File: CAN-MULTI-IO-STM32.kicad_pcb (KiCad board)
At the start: 2 copper layers, 81 x 55 mm, 42 parts, among them J1 H GND L, J2 TERM, J3 UART1, J4 SWLINK, J5 PWR IN, U1 STM32L433RCT3, U2 MCP2562-E-SN

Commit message: schematic and layout refinement
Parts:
- removed CONSW3, CONSW4: Conn_01x05, Connector_PinHeader_2.54mm:PinHeader_1x05_P2.54mm_Horizontal
- added I2C2: G SCL SDA 3V, Connector_PinHeader_2.54mm:PinHeader_1x04_P2.54mm_Horizontal, F.Cu at (139.2, 88.0)
- added J7: I2C PU EN, Connector_PinHeader_2.54mm:PinHeader_1x02_P2.54mm_Vertical, F.Cu at (149.1, 92.0)
- added ONEWIRE1: G OW 3V, Connector_PinHeader_2.54mm:PinHeader_1x03_P2.54mm_Horizontal, F.Cu at (154.5, 88.0)
- added RPU1: 4K7, Resistor_SMD:R_0603_1608Metric_Pad0.98x0.95mm_HandSolder, F.Cu at (145.3, 91.0)
- added RPU2: 4K7, Resistor_SMD:R_0603_1608Metric_Pad0.98x0.95mm_HandSolder, F.Cu at (145.3, 92.8)
- added RPU3: 4K7, Resistor_SMD:R_0603_1608Metric_Pad0.98x0.95mm_HandSolder, F.Cu at (159.0, 90.8)
- renumbered ANA_IN1 to ADIO1, ANA_IN2 to ADIO2
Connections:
- U1 pad 17: /ADC1_IN8 -> unconnected-(U1-PA3-Pad17)
- U1 pad 20: /ADC1_IN9 -> unconnected-(U1-PA4-Pad20)
- U1 pad 21: /ADC1_IN10 -> unconnected-(U1-PA5-Pad21)
- U1 pad 22: /ADC1_IN11 -> unconnected-(U1-PA6-Pad22)
- U1 pad 23: /ADC1_IN12 -> unconnected-(U1-PA7-Pad23)
- U1 pad 24: unconnected-(U1-PC4-Pad24) -> /ONEW
- U1 pad 29: unconnected-(U1-PB10-Pad29) -> /I2C2_SCL
- U1 pad 30: unconnected-(U1-PB11-Pad30) -> /I2C2_SDA
- U1 pad 50: /DEN4 -> unconnected-(U1-PA15-Pad50)
- U1 pad 52: /CTL4 -> unconnected-(U1-PC11-Pad52)
- U1 pad 54: /DEN3 -> unconnected-(U1-PD2-Pad54)
- U1 pad 57: /CTL3 -> unconnected-(U1-PB5-Pad57)
- U1 pad 61: /CTL2 -> unconnected-(U1-PB8-Pad61)
- U1 pad 62: /DEN2 -> unconnected-(U1-PB9-Pad62)
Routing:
- net +3.3V: track 163.5 -> 207.8 mm
- net /ONEW: track 0.00 -> 32.0 mm, vias 0 -> 1
- net /I2C2_SCL: track 0.00 -> 25.9 mm, vias 0 -> 1
- net /I2C2_SDA: track 0.00 -> 23.4 mm, vias 0 -> 1
- net Net-(J7-Pin_1): track 0.00 -> 4.99 mm
- net /ADC1_IN10: track 1.72 -> 0.00 mm, vias 1 -> 0
- net /ADC1_IN12: track 1.69 -> 0.00 mm, vias 1 -> 0
- net /ADC1_IN11: track 1.69 -> 0.00 mm, vias 1 -> 0
- net /ADC1_IN9: track 1.19 -> 0.00 mm, vias 1 -> 0
- net GND: vias 88 -> 106

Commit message: final tweaks
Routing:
- net GND: track 5.06 -> 0.00 mm
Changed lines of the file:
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@@
 		)
 	)
-	(segment
-		(start 137 94.75)
-		(end 137.25 94.5)
-		(width 0.254)
-		(layer "F.Cu")
-		(net 6)
-	)
-	(segment
-		(start 138.575 91.9)
-		(end 138.575 92.775)
-		(width 0.254)
-		(layer "F.Cu")
-		(net 6)
-	)
-	(segment
-		(start 137 95.9)
-		(end 137 94.75)
-		(width 0.254)
-		(layer "F.Cu")
-		(net 6)
-	)
-	(segment
-		(start 138.225 93.125)
-		(end 138.225 93.75)
-		(width 0.254)
-		(layer "F.Cu")
-		(net 6)
-	)
-	(segment
-		(start 137.95 94.5)
-		(end 138.225 94.225)
-		(width 0.254)
-		(layer "F.Cu")
-		(net 6)
-	)
-	(segment
-		(start 137.25 94.5)
-		(end 137.95 94.5)
-		(width 0.254)
-		(layer "F.Cu")
-		(net 6)
-	)
-	(segment
-		(start 138.575 92.775)
-		(end 138.225 93.125)
-		(width 0.254)
-		(layer "F.Cu")
-		(net 6)
-	)
-	(segment
-		(start 138.225 94.225)
-		(end 138.225 93.75)
-		(width 0.254)
-		(layer "F.Cu")
-		(net 6)
-	)
 	(via
 		(at 131.6 94.2)
@@
 	)
 	(via
-		(at 138 106)
-		(size 0.508)
-		(drill 0.254)
+		(at 138.078049 106.003804)
+		(size 0.508)
+		(drill 0.254)

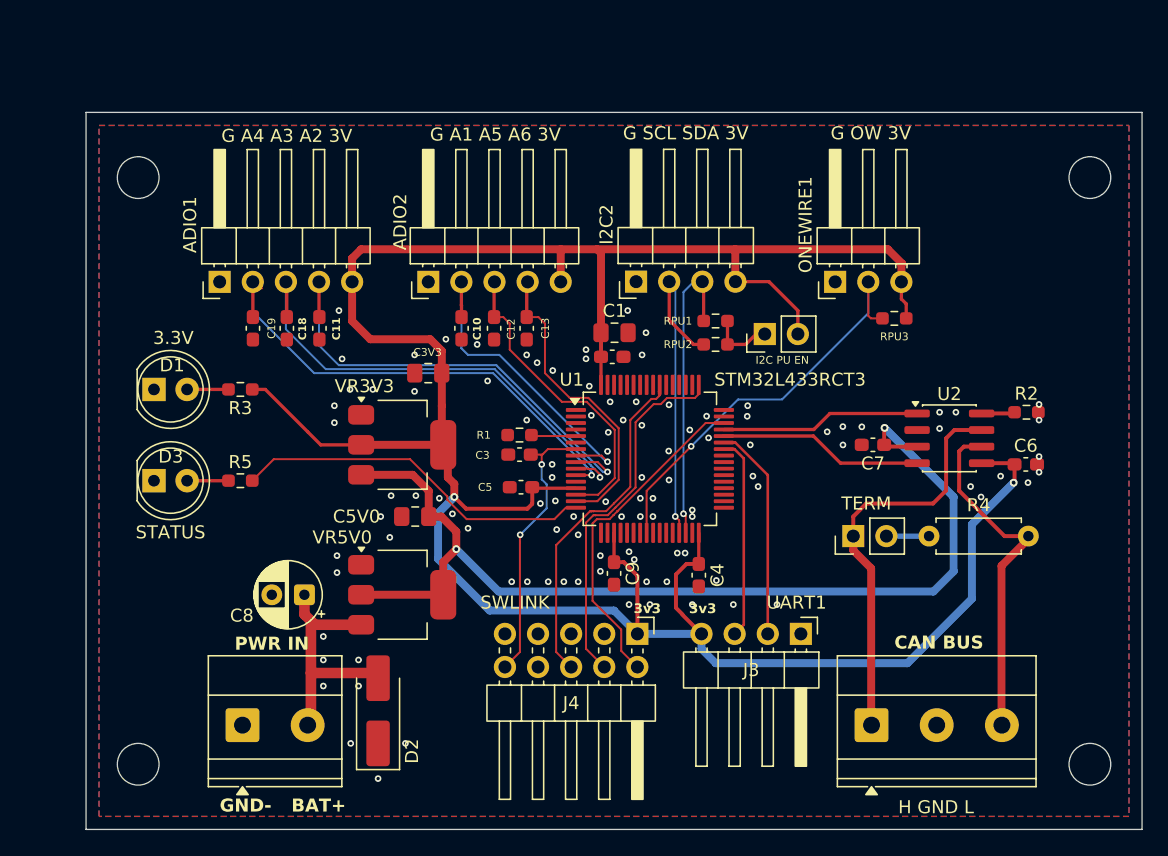
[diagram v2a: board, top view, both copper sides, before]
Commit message: optimized some connectors, switched to SMPS for 5v supply rail
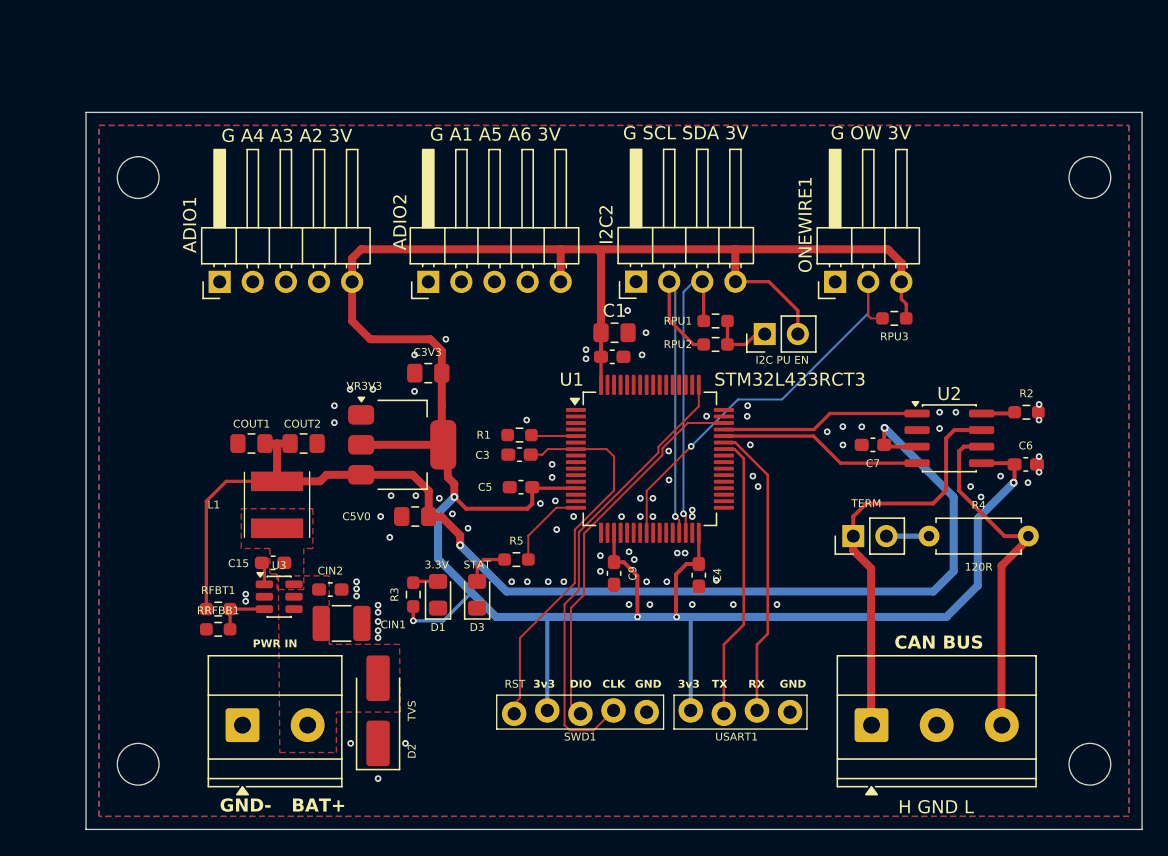
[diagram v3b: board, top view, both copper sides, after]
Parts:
- removed C10, C11, C12, C13, C18, C19: 100n, Capacitor_SMD:C_0603_1608Metric_Pad1.08x0.95mm_HandSolder
- removed C8: 10u, Capacitor_THT:CP_Radial_D5.0mm_P2.50mm
- removed J4: SWLINK, Connector_PinHeader_2.54mm:PinHeader_2x05_P2.54mm_Horizontal
- removed VR5V0: TLV1117-50, Package_TO_SOT_SMD:SOT-223-3_TabPin2
- added C15: 100n, Capacitor_SMD:C_0603_1608Metric_Pad1.08x0.95mm_HandSolder, F.Cu at (111.3, 109.5)
- added CIN1: 10u, Capacitor_SMD:C_1210_3225Metric_Pad1.33x2.70mm_HandSolder, F.Cu at (116.6, 114.2)
- added CIN2: 100n, Capacitor_SMD:C_0603_1608Metric_Pad1.08x0.95mm_HandSolder, F.Cu at (115.7, 111.6)
- added COUT1: 10u, Capacitor_SMD:C_0805_2012Metric_Pad1.18x1.45mm_HandSolder, F.Cu at (109.7, 100.4)
- added COUT2: 10u, Capacitor_SMD:C_0805_2012Metric_Pad1.18x1.45mm_HandSolder, F.Cu at (113.7, 100.4)
- added L1: VLS5045EX-100M-H, SamacSys_Parts:VLS5045EX330M, F.Cu at (111.7, 105.1)
- added RFBT1: 115K, Resistor_SMD:R_0603_1608Metric_Pad0.98x0.95mm_HandSolder, F.Cu at (107.1, 113.1)
- added RRFBB1: 22K1, Resistor_SMD:R_0603_1608Metric_Pad0.98x0.95mm_HandSolder, F.Cu at (107.1, 114.7)
- added SWD1: STLINK, PCM_SparkFun-Connector:1x05_P2.54mm_Locking, F.Cu at (140.0, 121.0)
- added U3: LMR54410, Package_TO_SOT_SMD:SOT-23-6, F.Cu at (111.8, 112.2)
- D1: footprint LED_THT:LED_D5.0mm_Clear -> LED_SMD:LED_0805_2012Metric_Pad1.15x1.40mm_HandSolder
- D3: value STATUS -> STAT; footprint LED_THT:LED_D5.0mm_Clear -> LED_SMD:LED_0805_2012Metric_Pad1.15x1.40mm_HandSolder
- J3: value UART1 -> USART1; footprint Connector_PinHeader_2.54mm:PinHeader_1x04_P2.54mm_Horizontal -> PCM_SparkFun-Connector:1x04_P2.54mm_Locking
- moved D1 26.9 mm to (124.0, 112.0), turned to 90 degrees
- moved D3 26.3 mm to (127.0, 112.0), turned to 90 degrees
- moved R5 22.0 mm to (130.0, 109.3)
- moved R3 20.6 mm to (122.1, 112.0), turned to 90 degrees
- moved J3 6.06 mm to (151.0, 121.0), turned to 180 degrees
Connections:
- ADIO1 pad 1: GND -> unconnected-(ADIO1-Pin_1-Pad1)
- ADIO1 pad 2: /ADC1_IN4 -> unconnected-(ADIO1-Pin_2-Pad2)
- ADIO1 pad 3: /ADC1_IN3 -> unconnected-(ADIO1-Pin_3-Pad3)
- ADIO1 pad 4: /ADC1_IN2 -> unconnected-(ADIO1-Pin_4-Pad4)
- ADIO1 pad 5: +3.3V -> unconnected-(ADIO1-Pin_5-Pad5)
- ADIO2 pad 1: GND -> unconnected-(ADIO2-Pin_1-Pad1)
- ADIO2 pad 2: /ADC1_IN1 -> unconnected-(ADIO2-Pin_2-Pad2)
- ADIO2 pad 3: /ADC1_IN5 -> unconnected-(ADIO2-Pin_3-Pad3)
- ADIO2 pad 4: /ADC1_IN6 -> unconnected-(ADIO2-Pin_4-Pad4)
- ADIO2 pad 5: +3.3V -> unconnected-(ADIO2-Pin_5-Pad5)
- U1 pad 10: /ADC1_IN3 -> unconnected-(U1-PC2-Pad10)
- U1 pad 11: /ADC1_IN4 -> unconnected-(U1-PC3-Pad11)
- U1 pad 14: /ADC1_IN5 -> unconnected-(U1-PA0-Pad14)
- U1 pad 15: /ADC1_IN6 -> unconnected-(U1-PA1-Pad15)
- U1 pad 8: /ADC1_IN1 -> unconnected-(U1-PC0-Pad8)
- U1 pad 9: /ADC1_IN2 -> unconnected-(U1-PC1-Pad9)
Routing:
- net /ADC1_IN4: track 38.6 -> 0.00 mm, vias 1 -> 0
- net /ADC1_IN3: track 37.5 -> 0.00 mm, vias 1 -> 0
- net /ADC1_IN2: track 36.5 -> 0.00 mm, vias 1 -> 0
- net /SWO: track 26.9 -> 0.52 mm
- net /ADC1_IN1: track 25.2 -> 0.00 mm, vias 1 -> 0
- net /ADC1_IN5: track 23.9 -> 0.00 mm
- net /ADC1_IN6: track 23.5 -> 0.00 mm
- net /STATUS: track 27.9 -> 6.37 mm
- net +12V: track 19.0 -> 0.35 mm
- net +5V: track 78.1 -> 94.3 mm
- net /NRST: track 21.4 -> 29.8 mm, vias 2 -> 0
- net /SWCLK: track 28.0 -> 34.9 mm
- net /USART1_TX: track 15.6 -> 22.0 mm
- net /USART1_RX: track 16.6 -> 22.8 mm
- net Net-(U3-FB): track 0.00 -> 4.18 mm
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- added copper zone on F.Cu, net +12V
- added copper zone on F.Cu, net /SW
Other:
- board text added: "CLK"
- board text added: "DIO"
- board text added: "GND"
- board text added: "RST"
- board text added: "RX"
- board text added: "TX"

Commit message: added i2c adc and gpio chips to isolate the mcu, lots of layout work
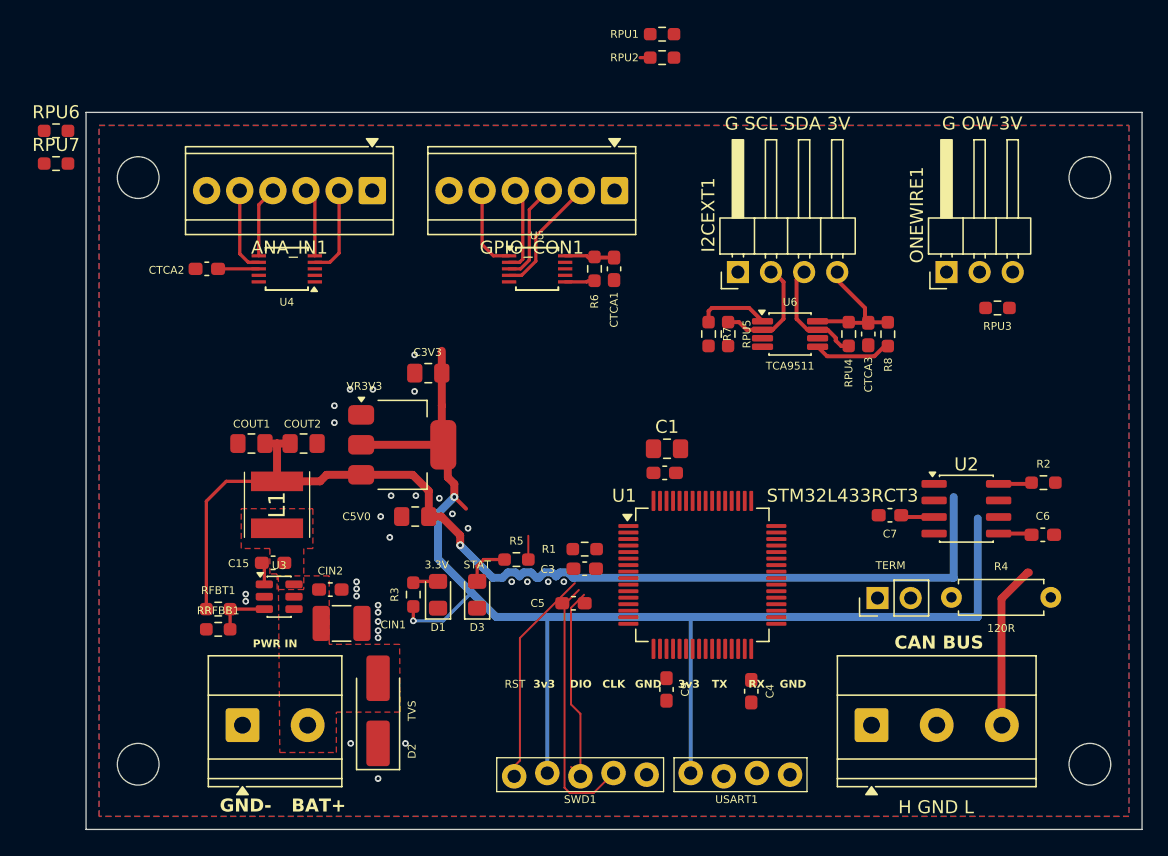
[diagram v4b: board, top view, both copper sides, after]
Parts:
- removed ADIO1: G A4 A3 A2 3V, Connector_PinHeader_2.54mm:PinHeader_1x05_P2.54mm_Horizontal
- removed ADIO2: G A1 A5 A6 3V, Connector_PinHeader_2.54mm:PinHeader_1x05_P2.54mm_Horizontal
- removed J7: I2C PU EN, Connector_PinHeader_2.54mm:PinHeader_1x02_P2.54mm_Vertical
- added ANA_IN1: Conn_01x06, TerminalBlock_TE-Connectivity:TerminalBlock_TE_282834-6_1x06_P2.54mm_Horizontal, F.Cu at (119.0, 81.0)
- added CTCA1: 100n, Capacitor_SMD:C_0603_1608Metric_Pad1.08x0.95mm_HandSolder, F.Cu at (137.5, 87.0)
- added CTCA2: 100n, Capacitor_SMD:C_0603_1608Metric_Pad1.08x0.95mm_HandSolder, F.Cu at (106.3, 87.0)
- added CTCA3: 100n, Capacitor_SMD:C_0603_1608Metric_Pad1.08x0.95mm_HandSolder, F.Cu at (157.0, 92.0)
- added GPIO_CON1: Conn_01x06, TerminalBlock_TE-Connectivity:TerminalBlock_TE_282834-6_1x06_P2.54mm_Horizontal, F.Cu at (137.5, 81.0)
- added R6: 10K, Resistor_SMD:R_0603_1608Metric_Pad0.98x0.95mm_HandSolder, F.Cu at (136.0, 87.0)
- added R7: 10K, Resistor_SMD:R_0603_1608Metric_Pad0.98x0.95mm_HandSolder, F.Cu at (144.8, 92.0)
- added R8: 10K, Resistor_SMD:R_0603_1608Metric_Pad0.98x0.95mm_HandSolder, F.Cu at (158.5, 92.0)
- added RPU4: 4K7, Resistor_SMD:R_0603_1608Metric_Pad0.98x0.95mm_HandSolder, F.Cu at (155.5, 92.0)
- added RPU5: 4K7, Resistor_SMD:R_0603_1608Metric_Pad0.98x0.95mm_HandSolder, F.Cu at (146.2, 92.0)
- added RPU6: 10K, Resistor_SMD:R_0603_1608Metric_Pad0.98x0.95mm_HandSolder, F.Cu at (94.7, 76.4)
- added RPU7: 10K, Resistor_SMD:R_0603_1608Metric_Pad0.98x0.95mm_HandSolder, F.Cu at (94.7, 78.9)
- added U4: ADS1015IDGS, Package_SO:TSSOP-10_3x3mm_P0.5mm, F.Cu at (112.4, 87.0)
- added U5: PCA9537, Package_SO:TSSOP-10_3x3mm_P0.5mm, F.Cu at (131.6, 87.0)
- added U6: TCA9511, Package_SO:VSSOP-8_3x3mm_P0.65mm, F.Cu at (151.0, 92.0)
- RPU1, RPU2: value 4K7 -> 10K
- moved RPU1 22.4 mm to (141.2, 69.0)
- moved RPU2 22.4 mm to (141.2, 70.8)
- moved C3 10.1 mm to (135.2, 110.0)
- moved R1 10.1 mm to (135.2, 108.5)
- moved C4 9.77 mm to (148.0, 119.4)
- moved C9 9.77 mm to (141.5, 119.3)
- moved C2 9.77 mm to (141.4, 102.7)
- moved C5 9.77 mm to (134.4, 112.7)
- moved C1 9.77 mm to (141.6, 100.8)
- moved U1 9.77 mm to (144.3, 110.5)
- moved ONEWIRE1 8.57 mm to (163.0, 87.2)
- moved RPU3 7.95 mm to (166.9, 90.0)
- moved I2CEXT1 7.84 mm to (147.0, 87.2)
- moved C7 5.56 mm to (158.7, 105.9)
- moved R2 5.56 mm to (170.4, 103.4)
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- renumbered I2C2 to I2CEXT1
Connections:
- I2CEXT1 pad 2: /I2C2_SCL -> /SCLOUT
- I2CEXT1 pad 3: /I2C2_SDA -> /SDAOUT
- RPU1 pad 2: Net-(J7-Pin_1) -> +3.3V
- RPU2 pad 2: Net-(J7-Pin_1) -> +3.3V
- U1 pad 55: /SWO -> unconnected-(U1-PB3-Pad55)
- U1 pad 61: unconnected-(U1-PB8-Pad61) -> /I2C1_SCL
- U1 pad 62: unconnected-(U1-PB9-Pad62) -> /I2C1_SDA
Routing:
- net +3.3V: track 211.2 -> 125.0 mm, vias 5 -> 2
- net /ONEW: track 32.0 -> 0.00 mm, vias 1 -> 0
- net /CANH: track 31.5 -> 0.00 mm
- net /I2C2_SCL: track 25.9 -> 0.78 mm, vias 1 -> 0
- net /I2C2_SDA: track 23.4 -> 0.00 mm, vias 1 -> 0
- net /USART1_RX: track 22.8 -> 0.00 mm
- net /USART1_TX: track 22.0 -> 0.00 mm
- net /CAN1_RX: track 15.7 -> 0.00 mm
- net /CAN1_TX: track 15.3 -> 0.00 mm
- net /SWCLK: track 34.9 -> 20.2 mm
- net /CANL: track 27.0 -> 12.6 mm
- net /SWDIO: track 29.1 -> 15.7 mm
- net /NRST: track 29.8 -> 16.7 mm
- net Net-(GPIO_CON1-Pin_2): track 0.00 -> 9.36 mm
- net /SCLOUT: track 0.00 -> 8.95 mm
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
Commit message: lots of progress, lots to do
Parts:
- added CAIN0: 100n, Capacitor_SMD:C_0603_1608Metric_Pad1.08x0.95mm_HandSolder, F.Cu at (118.3, 89.4)
- added CAIN1: 100n, Capacitor_SMD:C_0603_1608Metric_Pad1.08x0.95mm_HandSolder, F.Cu at (114.4, 89.4)
- added CAIN2: 100n, Capacitor_SMD:C_0603_1608Metric_Pad1.08x0.95mm_HandSolder, F.Cu at (111.5, 86.0)
- added CAIN3: 100n, Capacitor_SMD:C_0603_1608Metric_Pad1.08x0.95mm_HandSolder, F.Cu at (111.5, 87.8)
- moved RPU6 50.2 mm to (139.6, 98.8), turned to 180 degrees
- moved RPU7 49.5 mm to (140.6, 97.3), turned to 180 degrees
- moved RPU1 28.8 mm to (153.6, 95.0)
- moved RPU2 25.4 mm to (148.9, 95.0), turned to 180 degrees
- moved U4 6.37 mm to (106.2, 88.5), turned to 90 degrees
- moved CTCA2 3.17 mm to (103.2, 86.2), turned to -90 degrees
- moved R5 3.01 mm to (128.9, 112.1), turned to -90 degrees
- moved C1 2.12 mm to (139.4, 100.8), turned to 180 degrees
- moved C2 2.12 mm to (139.3, 102.7), turned to 180 degrees
- moved R8 1.50 mm to (157.0, 92.0)
- moved CTCA3 1.50 mm to (158.5, 92.0)
- moved C5 0.86 mm to (135.2, 112.8)
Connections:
- net Net-(ANA_IN1-Pin_2) renamed /AIN0
- net Net-(ANA_IN1-Pin_3) renamed /AIN1
- net Net-(ANA_IN1-Pin_4) renamed /AIN2
- net Net-(ANA_IN1-Pin_5) renamed /AIN3
- J3 pad 2: /USART1_RX -> /USART1_TX
- J3 pad 3: /USART1_TX -> /USART1_RX
- U1 pad 51: unconnected-(U1-PC10-Pad51) -> /TCA_RDY
- U1 pad 52: unconnected-(U1-PC11-Pad52) -> /TCA_EN
- U4 pad 1: /I2C1_SCL -> GND
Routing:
- net +3.3V: track 125.0 -> 303.2 mm, vias 2 -> 12
- net /I2C1_SCL: track 0.00 -> 62.9 mm, vias 0 -> 2
- net /I2C1_SDA: track 0.00 -> 62.1 mm
- net /I2C2_SDA: track 0.00 -> 28.0 mm
- net /I2C2_SCL: track 0.78 -> 28.0 mm
- net /CANH: track 0.00 -> 24.7 mm
- net /USART1_RX: track 0.00 -> 20.0 mm
- net /USART1_TX: track 0.00 -> 18.1 mm
- net /SWDIO: track 15.7 -> 33.3 mm
- net /TCA_EN: track 5.50 -> 22.1 mm
- net /AIN0: track 6.94 -> 22.2 mm
- net /TCA_RDY: track 5.76 -> 20.5 mm, vias 0 -> 2
- net /AIN1: track 5.28 -> 16.8 mm
- net /NRST: track 16.7 -> 28.3 mm
- net /CANL: track 12.6 -> 23.4 mm
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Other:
- board text added: "(C) 2026 G MCLELLAN CAN MULTI-IO INTERFACE REV 01"
- board text removed: "(C) 2026 G MCLELLAN STM32 QUAD SWITCH CONTROL REV 01"
